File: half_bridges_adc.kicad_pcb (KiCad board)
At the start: 2 copper layers, 76.2 x 55.3 mm, 36 parts, among them IC1 TSC213IYCT, IC2 LF2304NTR, IC3 TSC213IYCT, IC4 TSC213IYCT, J1 Conn_02x19_Odd_Even, J2 Conn_02x19_Odd_Even, J3 Screw_Terminal_01x02, J4 Screw_Terminal_01x02, J5 Screw_Terminal_01x02, J6 Screw_Terminal_01x02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

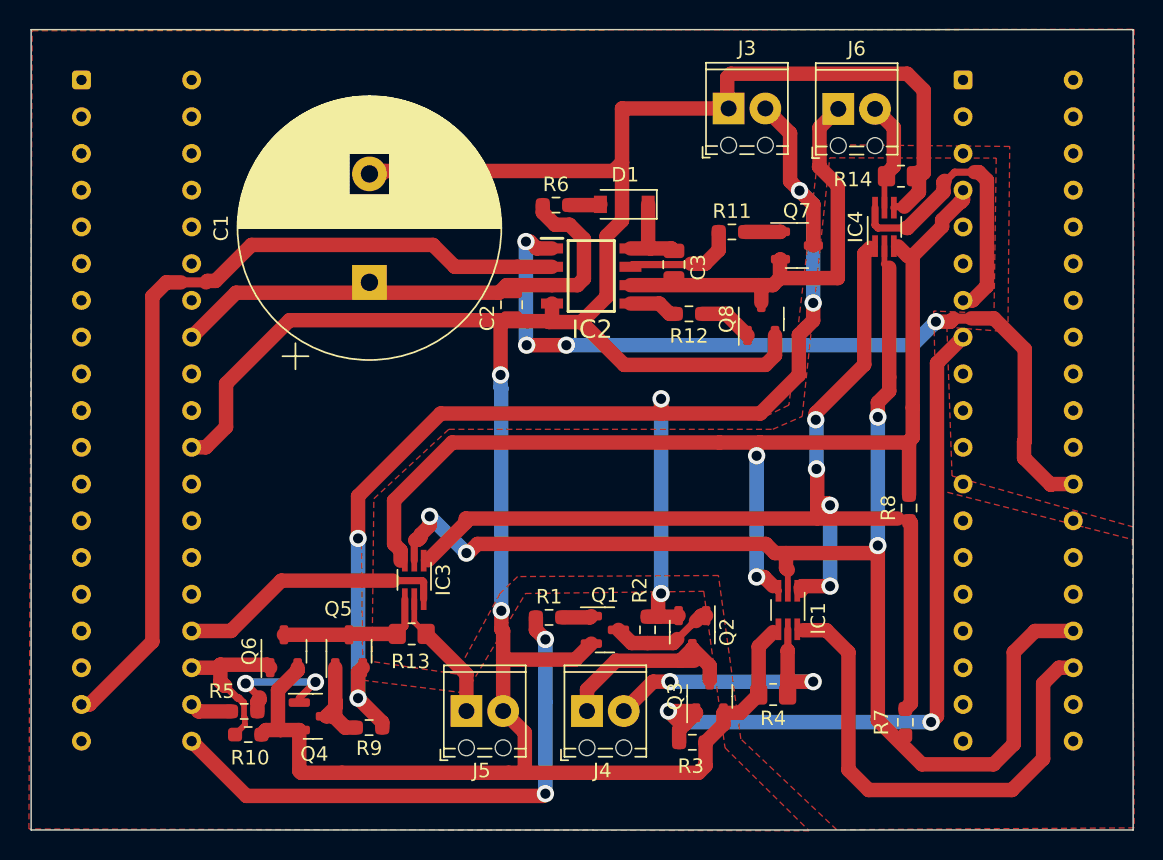
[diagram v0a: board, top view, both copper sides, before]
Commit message: minimum clearance 0 -> 0.25mm
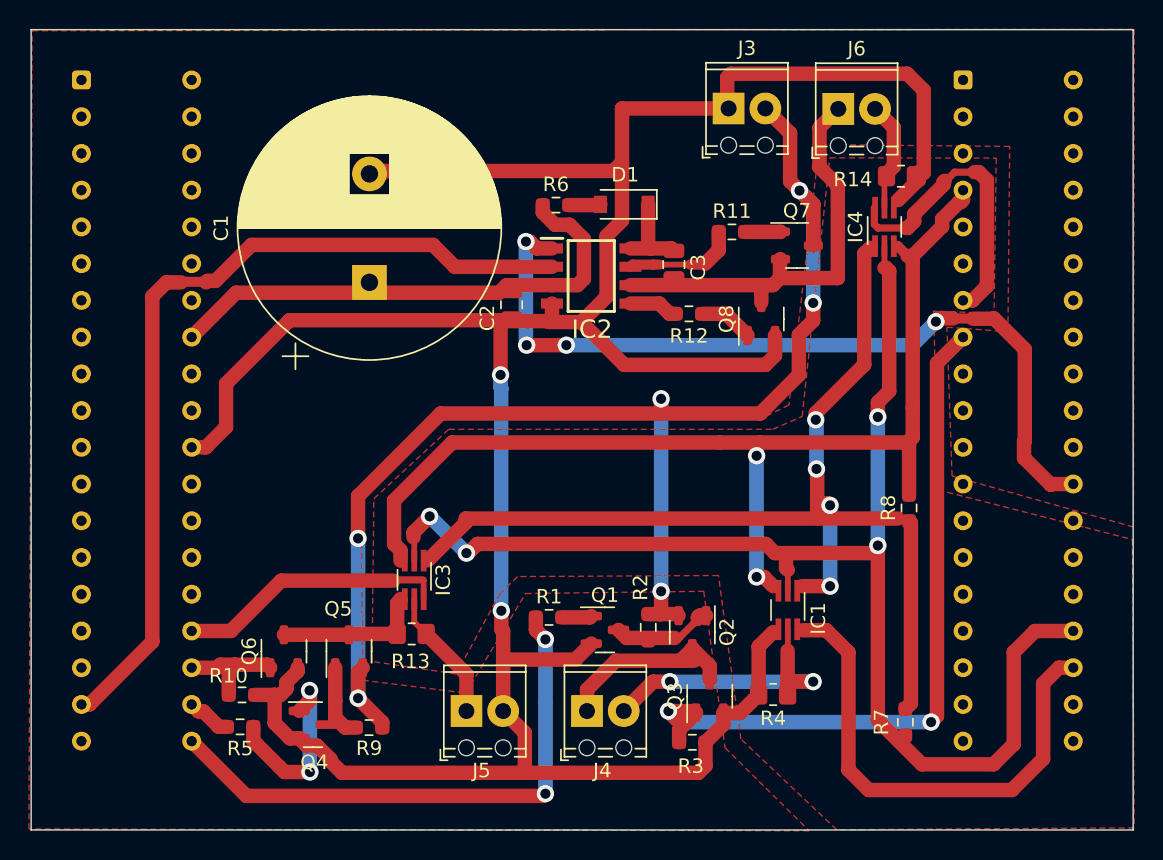
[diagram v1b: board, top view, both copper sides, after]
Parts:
- moved R10 2.78 mm to (111.1, 142.5)
- moved R5 1.10 mm to (111.0, 144.7)
- moved Q4 0.58 mm to (116.0, 144.6)
- moved R2 0.18 mm to (139.2, 137.8)
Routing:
- net Net-(Q4-Pad1): track 9.14 -> 13.1 mm
- net Net-(J1-Pad34): track 11.5 -> 7.86 mm
- net Net-(Q4-Pad3): track 8.15 -> 5.20 mm
- net /GND: track 206.6 -> 204.5 mm
- net /AVCC: track 77.1 -> 76.5 mm
- net /AGND: track 94.5 -> 93.9 mm
- net Net-(Q1-Pad3): track 7.22 -> 6.64 mm

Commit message: fix: move right connextor 2.54mm to the right
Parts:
- moved J2 2.54 mm to (163.5, 100.0)
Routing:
- net /GND: track 204.5 -> 169.0 mm
- net Net-(IC4-Pad6): track 20.7 -> 23.6 mm
- net /AGND: track 93.9 -> 91.3 mm
- net Net-(J2-Pad15): track 52.0 -> 54.2 mm
- net Net-(IC1-Pad6): track 35.0 -> 37.0 mm
- net /AVCC: track 76.5 -> 78.4 mm
- net Net-(IC2-Pad1): track 57.0 -> 58.6 mm
